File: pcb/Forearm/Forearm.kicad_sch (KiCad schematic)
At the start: 19 parts, among them J1 Conn_01x02, J2 Conn_01x12_Ribbon_To_Top, J3 Conn_01x12_To_Bottom, J9 Conn_01x01, U1 ESP32-S3-DEVKITC-1-N8R2, U2 4754

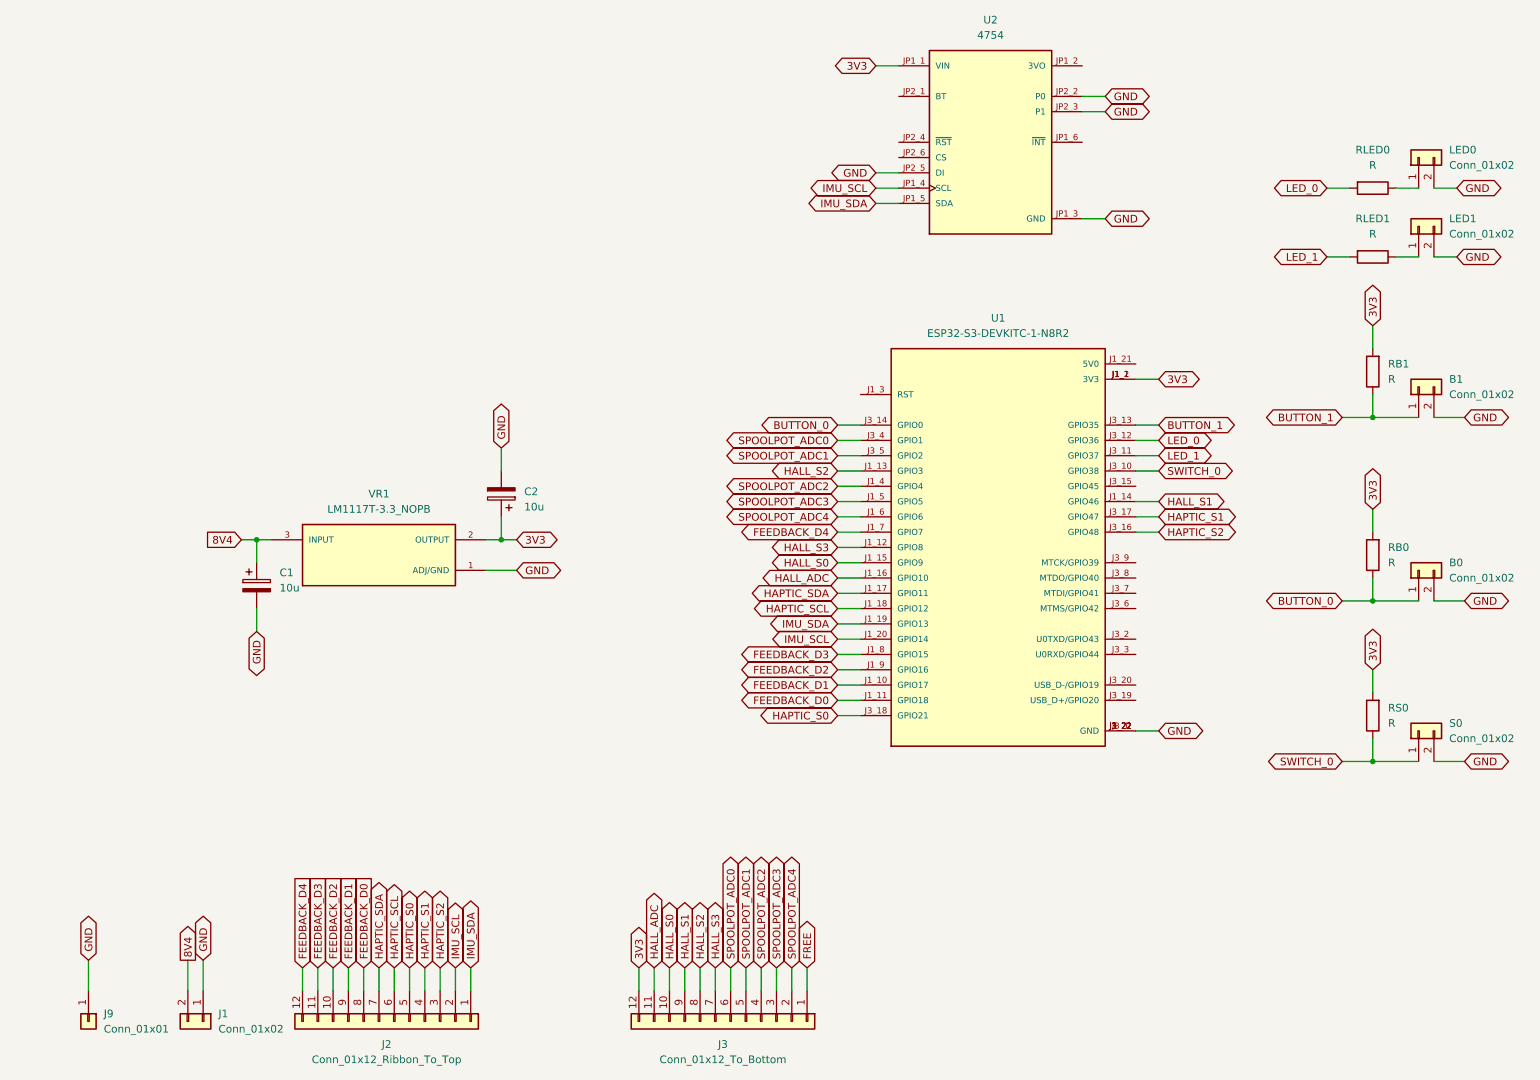
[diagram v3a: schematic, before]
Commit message: re-work of pcbs for pin issues in progress 1
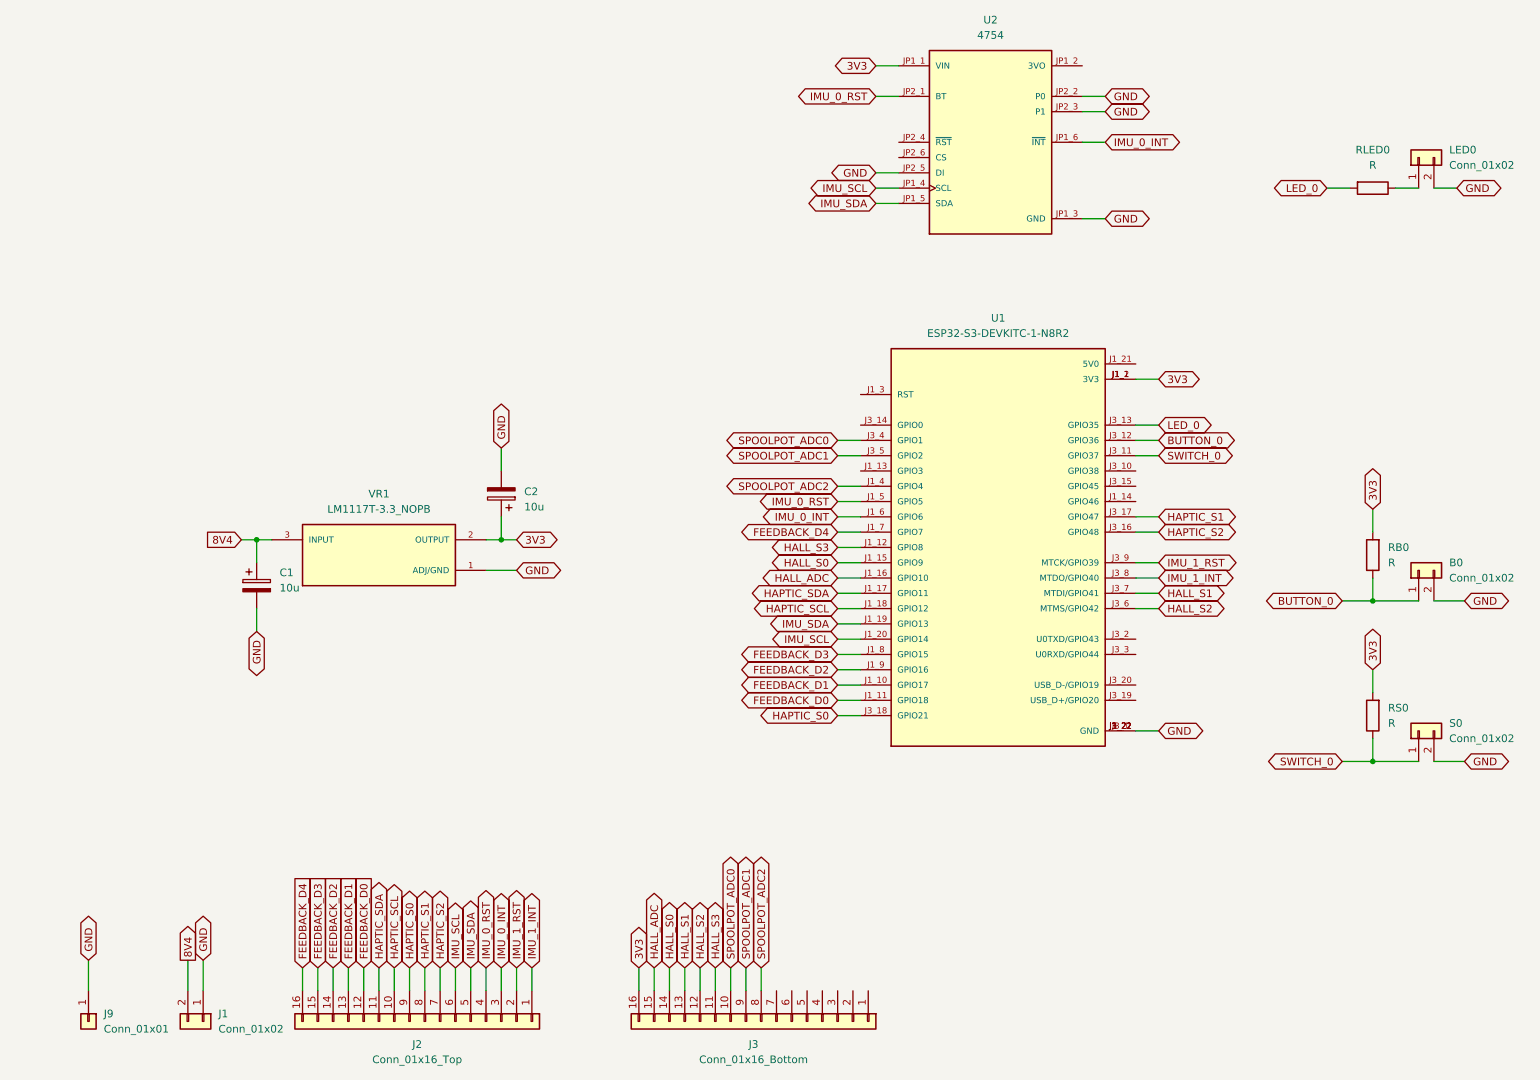
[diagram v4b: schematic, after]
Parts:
- removed B1, LED1: Conn_01x02, Connector_PinSocket_2.54mm:PinSocket_1x02_P2.54mm_Vertical, symbol Connector_Generic:Conn_01x02
- removed J2: Conn_01x12_Ribbon_To_Top, 0522071233:0522071233, symbol Connector_Generic:Conn_01x12
- removed J3: Conn_01x12_To_Bottom, 0522071233:0522071233, symbol Connector_Generic:Conn_01x12
- removed RB1, RLED1: R, Resistor_SMD:R_0402_1005Metric, symbol Device:R
- added J2: Conn_01x16_Top, 522071633:CON_522071633_MOL, symbol Connector_Generic:Conn_01x16
- added J3: Conn_01x16_Bottom, 522071633:CON_522071633_MOL, symbol Connector_Generic:Conn_01x16
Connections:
- net BUTTON_1 is gone; now on net LED_0: U1.J3_13 (GPIO35)
- net LED_1 is gone; now on net SWITCH_0: U1.J3_11 (GPIO37)
- net SPOOLPOT_ADC3 is gone; now on net IMU_0_RST: U1.J1_5 (GPIO5)
- net SPOOLPOT_ADC4 is gone; now on net IMU_0_INT: U1.J1_6 (GPIO6)
- net 3V3: now also J3.16 (Pin_16)
- net BUTTON_0: now also U1.J3_12 (GPIO36); no longer U1.J3_14 (GPIO0)
- net FEEDBACK_D0: now also J2.12 (Pin_12)
- net FEEDBACK_D1: now also J2.13 (Pin_13)
- net FEEDBACK_D2: now also J2.14 (Pin_14)
- net FEEDBACK_D3: now also J2.15 (Pin_15)
- net FEEDBACK_D4: now also J2.16 (Pin_16)
- net HALL_ADC: now also J3.15 (Pin_15)
- net HALL_S0: now also J3.14 (Pin_14)
- net HALL_S1: now also U1.J3_7 (MTDI/GPIO41), J3.13 (Pin_13); no longer U1.J1_14 (GPIO46)
- net HALL_S2: now also U1.J3_6 (MTMS/GPIO42), J3.12 (Pin_12); no longer U1.J1_13 (GPIO3)
- net HALL_S3: now also J3.11 (Pin_11)
- net HAPTIC_S0: now also J2.9 (Pin_9)
- net HAPTIC_S1: now also J2.8 (Pin_8)
- net HAPTIC_S2: now also J2.7 (Pin_7)
- net HAPTIC_SCL: now also J2.10 (Pin_10)
- net HAPTIC_SDA: now also J2.11 (Pin_11)
- net IMU_SCL: now also J2.6 (Pin_6)
- net IMU_SDA: now also J2.5 (Pin_5)
- net LED_0: no longer U1.J3_12 (GPIO36)
- net SPOOLPOT_ADC0: now also J3.10 (Pin_10)
- net SPOOLPOT_ADC1: now also J3.9 (Pin_9)
- net SPOOLPOT_ADC2: now also J3.8 (Pin_8)
- net SWITCH_0: no longer U1.J3_10 (GPIO38)
- net IMU_1_INT: now reaches U1.J3_8 (MTDO/GPIO40)
- net IMU_1_INT: now also J2.1 (Pin_1)
- net IMU_1_RST: now reaches U1.J3_9 (MTCK/GPIO39)
- net IMU_1_RST: now also J2.2 (Pin_2)
- net IMU_0_INT: now reaches U2.JP1_6 (~{INT})
- net IMU_0_INT: now also J2.3 (Pin_3)
- net IMU_0_RST: now reaches U2.JP2_1 (BT)
- net IMU_0_RST: now also J2.4 (Pin_4)

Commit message: revised pcbs in prep for manufacture, rev2
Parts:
- added B1, LED1: Conn_01x02, Connector_PinSocket_2.54mm:PinSocket_1x02_P2.54mm_Vertical, symbol Connector_Generic:Conn_01x02
- added RB1, RLED1: R, Resistor_SMD:R_0402_1005Metric, symbol Device:R
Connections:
- net 3V3: now also RB1.2
- net BUTTON_0: now also U1.J3_11 (GPIO37); no longer U1.J3_12 (GPIO36)
- net GND: now also B1.2 (Pin_2), LED1.2 (Pin_2)
- net HALL_S1: now also U1.J1_14 (GPIO46); no longer U1.J3_7 (MTDI/GPIO41)
- net HALL_S2: now also U1.J1_13 (GPIO3); no longer U1.J3_6 (MTMS/GPIO42)
- net HAPTIC_S0: now also J2.11 (Pin_11); no longer J2.9 (Pin_9)
- net HAPTIC_S1: now also J2.10 (Pin_10); no longer J2.8 (Pin_8)
- net HAPTIC_S2: now also J2.9 (Pin_9), U1.J3_13 (GPIO35); no longer J2.7 (Pin_7), U1.J3_16 (GPIO48)
- net HAPTIC_SCL: now also J2.7 (Pin_7), U1.J1_17 (GPIO11); no longer J2.10 (Pin_10), U1.J1_18 (GPIO12)
- net HAPTIC_SDA: now also J2.8 (Pin_8), U1.J1_18 (GPIO12); no longer J2.11 (Pin_11), U1.J1_17 (GPIO11)
- net IMU_0_INT: now also U1.J3_6 (MTMS/GPIO42); no longer J2.3 (Pin_3), U1.J1_6 (GPIO6)
- net IMU_0_RST: now also U1.J3_7 (MTDI/GPIO41); no longer J2.4 (Pin_4), U1.J1_5 (GPIO5)
- net IMU_1_INT: now also J2.3 (Pin_3); no longer J2.1 (Pin_1)
- net IMU_1_RST: now also J2.4 (Pin_4); no longer J2.2 (Pin_2)
- net IMU_SCL: now also U1.J1_19 (GPIO13); no longer U1.J1_20 (GPIO14)
- net IMU_SDA: now also U1.J1_20 (GPIO14); no longer U1.J1_19 (GPIO13)
- net LED_0: now also U1.J3_14 (GPIO0); no longer U1.J3_13 (GPIO35)
- net SWITCH_0: now also U1.J3_10 (GPIO38); no longer U1.J3_11 (GPIO37)
- net LED_1: now reaches U1.J3_15 (GPIO45)
- net LED_1: now also RLED1.2
- net SPOOLPOT_ADC4: now reaches J3.6 (Pin_6)
- net SPOOLPOT_ADC4: now also U1.J1_6 (GPIO6)
- net SPOOLPOT_ADC3: now reaches J3.7 (Pin_7)
- net SPOOLPOT_ADC3: now also U1.J1_5 (GPIO5)
- new net: LED1.1 (Pin_1), RLED1.1
- new net BUTTON_1: B1.1 (Pin_1), RB1.1, U1.J3_12 (GPIO36)

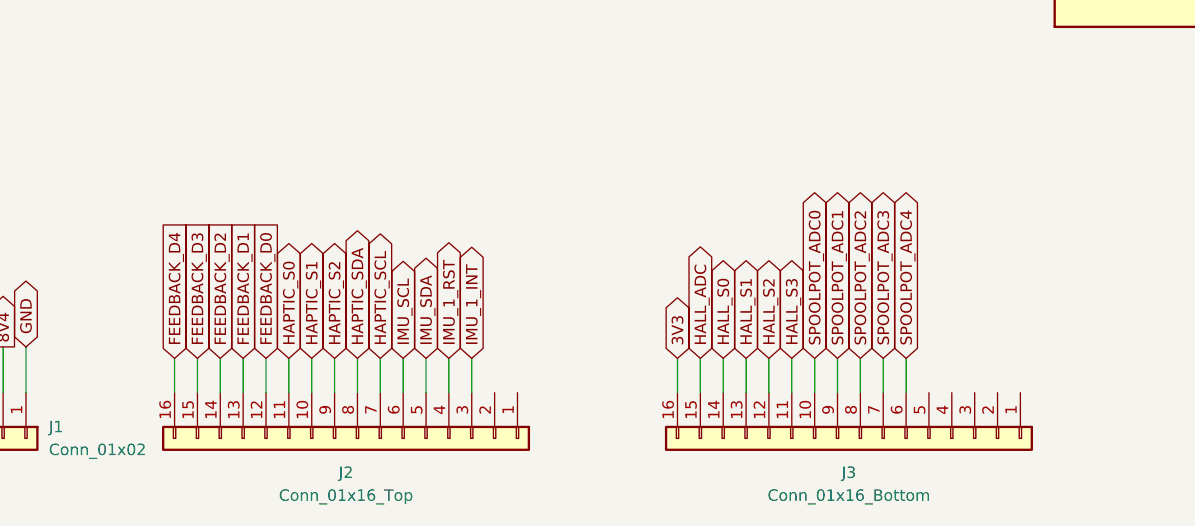
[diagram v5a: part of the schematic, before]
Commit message: added library files and updated forearm schematic
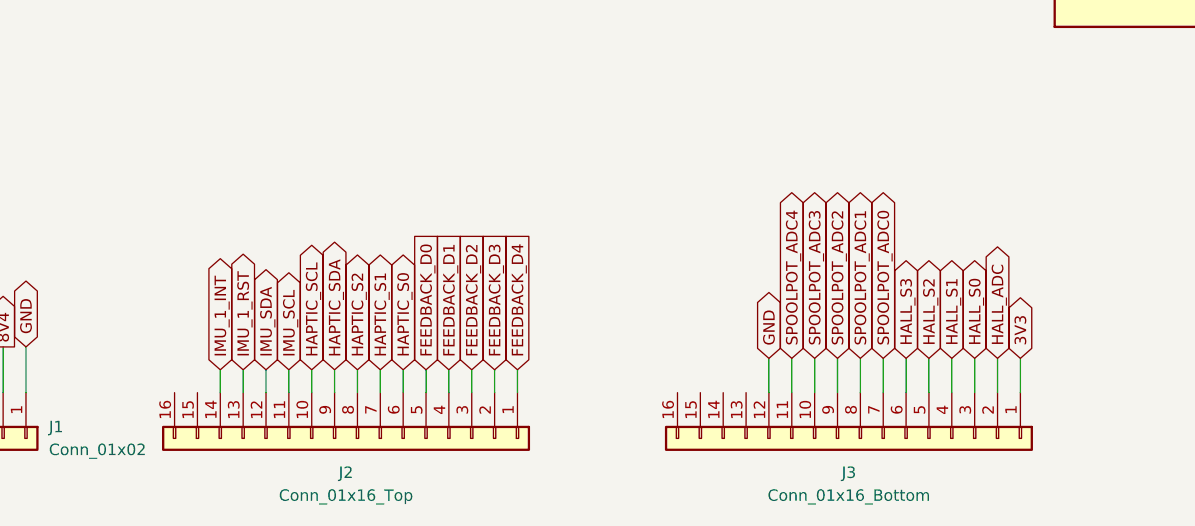
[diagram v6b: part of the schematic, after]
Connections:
- net 3V3: now also J3.1 (Pin_1); no longer J3.16 (Pin_16)
- net FEEDBACK_D0: now also J2.5 (Pin_5); no longer J2.12 (Pin_12)
- net FEEDBACK_D1: now also J2.4 (Pin_4); no longer J2.13 (Pin_13)
- net FEEDBACK_D2: now also J2.3 (Pin_3); no longer J2.14 (Pin_14)
- net FEEDBACK_D3: now also J2.2 (Pin_2); no longer J2.15 (Pin_15)
- net FEEDBACK_D4: now also J2.1 (Pin_1); no longer J2.16 (Pin_16)
- net GND: now also J3.12 (Pin_12)
- net HALL_ADC: now also J3.2 (Pin_2); no longer J3.15 (Pin_15)
- net HALL_S0: now also J3.3 (Pin_3); no longer J3.14 (Pin_14)
- net HALL_S1: now also J3.4 (Pin_4); no longer J3.13 (Pin_13)
- net HALL_S2: now also J3.5 (Pin_5); no longer J3.12 (Pin_12)
- net HALL_S3: now also J3.6 (Pin_6); no longer J3.11 (Pin_11)
- net HAPTIC_S0: now also J2.6 (Pin_6); no longer J2.11 (Pin_11)
- net HAPTIC_S1: now also J2.7 (Pin_7); no longer J2.10 (Pin_10)
- net HAPTIC_S2: now also J2.8 (Pin_8); no longer J2.9 (Pin_9)
- net HAPTIC_SCL: now also J2.10 (Pin_10); no longer J2.7 (Pin_7)
- net HAPTIC_SDA: now also J2.9 (Pin_9); no longer J2.8 (Pin_8)
- net IMU_1_INT: now also J2.14 (Pin_14); no longer J2.3 (Pin_3)
- net IMU_1_RST: now also J2.13 (Pin_13); no longer J2.4 (Pin_4)
- net IMU_SCL: now also J2.11 (Pin_11); no longer J2.6 (Pin_6)
- net IMU_SDA: now also J2.12 (Pin_12); no longer J2.5 (Pin_5)
- net SPOOLPOT_ADC0: now also J3.7 (Pin_7); no longer J3.10 (Pin_10)
- net SPOOLPOT_ADC1: now also J3.8 (Pin_8); no longer J3.9 (Pin_9)
- net SPOOLPOT_ADC2: now also J3.9 (Pin_9); no longer J3.8 (Pin_8)
- net SPOOLPOT_ADC3: now also J3.10 (Pin_10); no longer J3.7 (Pin_7)
- net SPOOLPOT_ADC4: now also J3.11 (Pin_11); no longer J3.6 (Pin_6)
